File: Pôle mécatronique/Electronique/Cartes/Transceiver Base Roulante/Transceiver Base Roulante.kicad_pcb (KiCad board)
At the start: 2 copper layers, 18.8 x 30.7 mm, 6 parts, among them J1 Conn_01x02, J3 Conn_01x01, J4 Conn_01x01, J6 Conn_01x02, U1 TCAN332

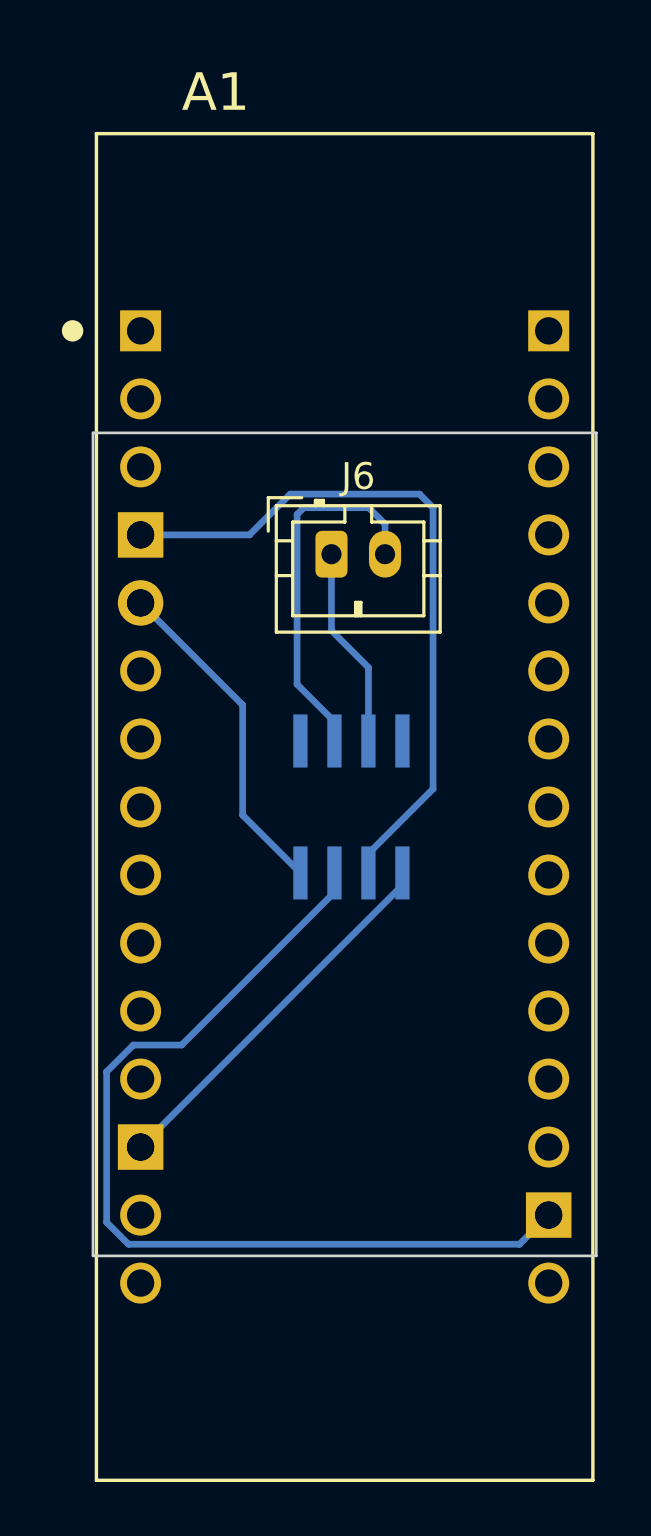
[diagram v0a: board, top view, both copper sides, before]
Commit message: Carte transceiver base roulante update
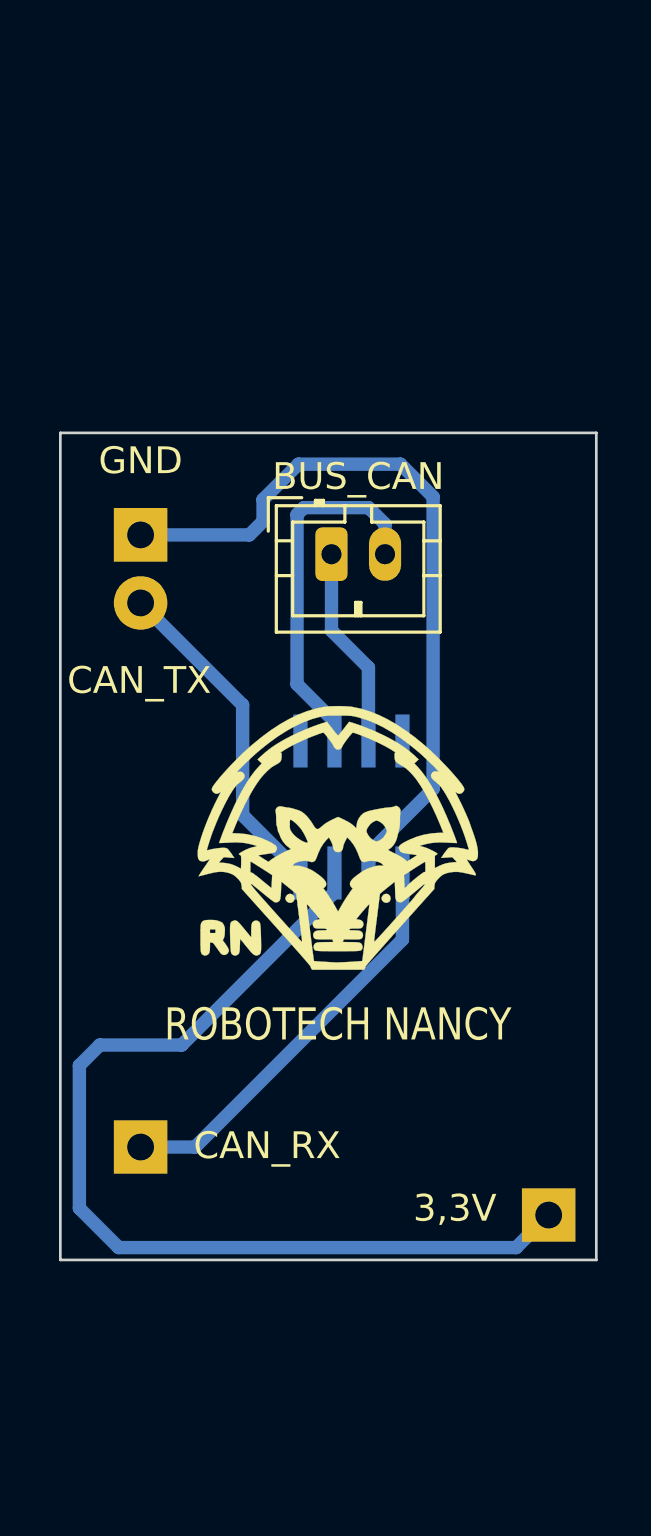
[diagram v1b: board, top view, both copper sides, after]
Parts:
- removed A1: NUCLEO-F303K8, empreinte:MODULE_NUCLEO-F303K8
- added G***: LOGO, Logos:logoRobotechNancy10x10, F.Cu at (154.4, 74.9)
- renumbered J3 to 3,3V, J6 to BUS_CAN, J4 to CAN_RX, J1 to GND
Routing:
- net +3V3: track 34.9 -> 36.9 mm
- net GND: track 26.4 -> 28.0 mm
- net CAN_RX: track 14.3 -> 15.5 mm
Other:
- board size 18.8 x 30.7 mm -> 20 x 30.9 mm
- board text added: "CAN_TX"
- board text added: "ROBOTECH NANCY"

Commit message: TCAN base roulante update
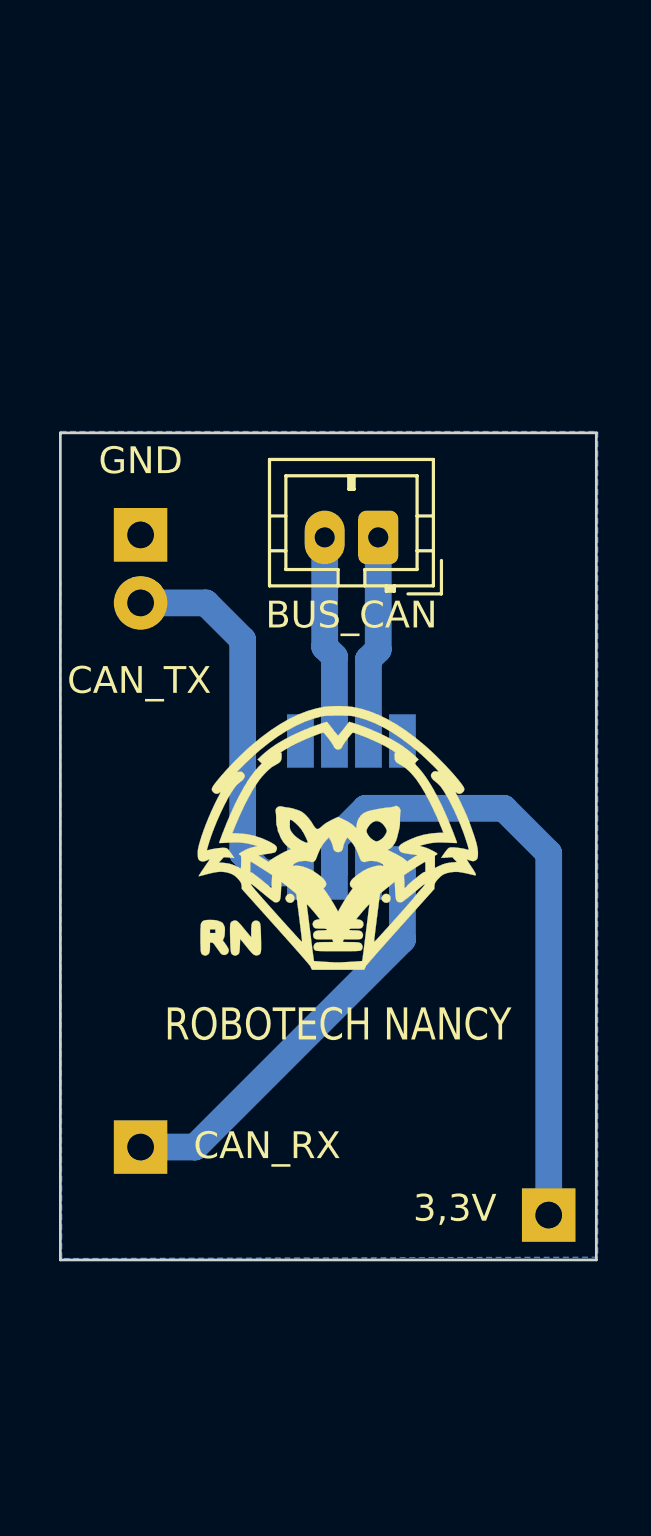
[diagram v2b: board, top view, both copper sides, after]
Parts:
- moved BUS_CAN 1.86 mm to (155.9, 63.8), turned to 180 degrees
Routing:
- net GND: track 28.0 -> 0.00 mm
- net +3V3: track 36.9 -> 23.9 mm
- net CAN_L: track 13.8 -> 7.75 mm
- net CAN_TX: track 12.6 -> 14.8 mm
- added copper zone on B.Cu, net GND
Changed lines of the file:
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@@
   )
   (setup
+    (stackup
+      (layer "F.SilkS" (type "Top Silk Screen"))
+      (layer "F.Paste" (type "Top Solder Paste"))
+      (layer "F.Mask" (type "Top Solder Mask") (thickness 0.01))
+      (layer "F.Cu" (type "copper") (thickness 0.035))
+      (layer "dielectric 1" (type "core") (thickness 1.51) (material "FR4") (epsilon_r 4.5) (loss_tangent 0.02))
+      (layer "B.Cu" (type "copper") (thickness 0.035))
+      (layer "B.Mask" (type "Bottom Solder Mask") (thickness 0.01))
+      (layer "B.Paste" (type "Bottom Solder Paste"))
+      (layer "B.SilkS" (type "Bottom Silk Screen"))
+      (copper_finish "None")
+      (dielectric_constraints no)
+    )
     (pad_to_mask_clearance 0)
     (pcbplotparams
@@
   (net 8 "unconnected-(U1-Pad8)")
   (footprint "Connector_JST:JST_PH_B2B-PH-K_1x02_P2.00mm_Vertical" (layer "F.Cu")
-    (at 154.194 64.474)
+    (at 155.94 63.8468 180)
     (descr "JST PH series connector, B2B-PH-K (http://www.jst-mfg.com/product/pdf/eng/ePH.pdf), generated with kicad-footprint-generator")
     (tags "connector JST PH side entry")
@@
     (fp_line (start -1.95 -1.7) (end -1.95 2.8) (layer "F.Fab") (width 0.1))
     (fp_line (start -1.11 -2.11) (end -2.36 -2.11) (layer "F.Fab") (width 0.1))
-    (pad "1" thru_hole roundrect locked (at 0 0) (size 1.2 2) (drill 0.75) (layers *.Cu *.Mask) (roundrect_rratio 0.208333)
+    (pad "1" thru_hole roundrect locked (at 0 0 180) (size 1.5 2) (drill 0.75) (layers *.Cu *.Mask) (roundrect_rratio 0.208333)
       (net 7 "CAN_H") (pinfunction "Pin_1") (pintype "passive"))
-    (pad "2" thru_hole oval locked (at 2 0) (size 1.2 2) (drill 0.75) (layers *.Cu *.Mask)
+    (pad "2" thru_hole oval locked (at 2 0 180) (size 1.5 2) (drill 0.75) (layers *.Cu *.Mask)
       (net 6 "CAN_L") (pinfunction "Pin_2") (pintype "passive"))
     (model "${KICAD6_3DMODEL_DIR}/Connector_JST.3dshapes/JST_PH_B2B-PH-K_1x02_P2.00mm_Vertical.wrl"
@@
     (fp_line (start 3.0988 0.4064) (end 3.0988 0.889) (layer "B.Fab") (width 0.1524))
     (fp_arc (start -0.3048 2.4892) (mid 0.0127 2.1971) (end 0.3048 2.5146) (layer "B.Fab") (width 0.1524))
-    (pad "1" smd rect locked (at -2.4638 1.905 90) (size 1.9812 0.5334) (layers "B.Cu" "B.Paste" "B.Mask")
+    (pad "1" smd rect locked (at -2.4638 1.905 90) (size 2 1) (layers "B.Cu" "B.Paste" "B.Mask")
       (net 2 "CAN_RX") (pinfunction "TXD") (pintype "input"))
-    (pad "2" smd rect locked (at -2.4638 0.635 90) (size 1.9812 0.5334) (layers "B.Cu" "B.Paste" "B.Mask")
+    (pad "2" smd rect locked (at -2.4638 0.635 90) (size 2 1) (layers "B.Cu" "B.Paste" "B.Mask")
       (net 1 "GND") (pinfunction "GND") (pintype "power_in"))
-    (pad "3" smd rect locked (at -2.4638 -0.635 90) (size 1.9812 0.5334) (layers "B.Cu" "B.Paste" "B.Mask")
+    (pad "3" smd rect locked (at -2.4638 -0.635 90) (size 2 1) (layers "B.Cu" "B.Paste" "B.Mask")
       (net 4 "+3V3") (pinfunction "VCC") (pintype "power_in"))
-    (pad "4" smd rect locked (at -2.4638 -1.905 90) (size 1.9812 0.5334) (layers "B.Cu" "B.Paste" "B.Mask")
+    (pad "4" smd rect locked (at -2.4638 -1.905 90) (size 2 1) (layers "B.Cu" "B.Paste" "B.Mask")
       (net 3 "CAN_TX") (pinfunction "RXD") (pintype "tri_state"))
-    (pad "5" smd rect locked (at 2.4638 -1.905 90) (size 1.9812 0.5334) (layers "B.Cu" "B.Paste" "B.Mask")
+    (pad "5" smd rect locked (at 2.4638 -1.905 90) (size 2 1) (layers "B.Cu" "B.Paste" "B.Mask")
       (net 5 "unconnected-(U1-Pad5)") (pinfunction "NC") (pintype "no_connect"))
-    (pad "6" smd rect locked (at 2.4638 -0.635 90) (size 1.9812 0.5334) (layers "B.Cu" "B.Paste" "B.Mask")
+    (pad "6" smd rect locked (at 2.4638 -0.635 90) (size 2 1) (layers "B.Cu" "B.Paste" "B.Mask")
       (net 6 "CAN_L") (pinfunction "CANL") (pintype "bidirectional"))
-    (pad "7" smd rect locked (at 2.4638 0.635 90) (size 1.9812 0.5334) (layers "B.Cu" "B.Paste" "B.Mask")
+    (pad "7" smd rect locked (at 2.4638 0.635 90) (size 2 1) (layers "B.Cu" "B.Paste" "B.Mask")
       (net 7 "CAN_H") (pinfunction "CANH") (pintype "bidirectional"))
-    (pad "8" smd rect locked (at 2.4638 1.905 90) (size 1.9812 0.5334) (layers "B.Cu" "B.Paste" "B.Mask")
+    (pad "8" smd rect locked (at 2.4638 1.905 90) (size 2 1) (layers "B.Cu" "B.Paste" "B.Mask")
       (net 8 "unconnected-(U1-Pad8)") (pinfunction "NC") (pintype "no_connect"))
     (model "C:/Users/tomro/OneDrive/Documents/Kicad/3D/LTC1329CS8-50#PBF.STEP"
@@
     (effects (font (size 1.2 1) (thickness 0.25)))
   )
-  (segment (start 152.9588 61.1124) (end 151.638 62.4332) (width 0.5) (layer "B.Cu") (net 1))
-  (segment (start 151.638 62.4332) (end 151.638 63.246) (width 0.5) (layer "B.Cu") (net 1))
-  (segment (start 155.575 75.6539) (end 157.988 73.2409) (width 0.5) (layer "B.Cu") (net 1))
-  (segment (start 156.7688 61.1124) (end 152.9588 61.1124) (width 0.5) (layer "B.Cu") (net 1))
-  (segment (start 151.638 63.246) (end 151.13 63.754) (width 0.5) (layer "B.Cu") (net 1))
-  (segment (start 157.988 73.2409) (end 157.988 62.3316) (width 0.5) (layer "B.Cu") (net 1))
-  (segment (start 157.988 62.3316) (end 156.7688 61.1124) (width 0.5) (layer "B.Cu") (net 1))
-  (segment (start 151.13 63.754) (end 147.066 63.754) (width 0.5) (layer "B.Cu") (net 1))
-  (segment (start 155.575 76.3778) (end 155.575 75.6539) (width 0.5) (layer "B.Cu") (net 1))
-  (segment (start 147.066 86.614) (end 149.098 86.614) (width 0.5) (layer "B.Cu") (net 2))
-  (segment (start 149.098 86.614) (end 156.845 78.867) (width 0.5) (layer "B.Cu") (net 2))
-  (segment (start 156.845 78.867) (end 156.845 76.3778) (width 0.5) (layer "B.Cu") (net 2))
-  (segment (start 150.876 70.104) (end 150.876 74.2188) (width 0.5) (layer "B.Cu") (net 3))
-  (segment (start 147.066 66.294) (end 150.876 70.104) (width 0.5) (layer "B.Cu") (net 3))
-  (segment (start 150.876 74.2188) (end 153.035 76.3778) (width 0.5) (layer "B.Cu") (net 3))
-  (segment (start 148.6027 82.804) (end 154.305 77.1017) (width 0.5) (layer "B.Cu") (net 4))
-  (segment (start 144.78 83.566) (end 145.542 82.804) (width 0.5) (layer "B.Cu") (net 4))
-  (segment (start 144.78 88.9) (end 144.78 83.566) (width 0.5) (layer "B.Cu") (net 4))
-  (segment (start 154.305 77.1017) (end 154.305 76.3778) (width 0.5) (layer "B.Cu") (net 4))
-  (segment (start 162.306 89.154) (end 161.091489 90.368511) (width 0.5) (layer "B.Cu") (net 4))
-  (segment (start 161.091489 90.368511) (end 146.248511 90.368511) (width 0.5) (layer "B.Cu") (net 4))
-  (segment (start 146.248511 90.368511) (end 144.78 88.9) (width 0.5) (layer "B.Cu") (net 4))
-  (segment (start 145.542 82.804) (end 148.6027 82.804) (width 0.5) (layer "B.Cu") (net 4))
-  (segment (start 155.583 62.738) (end 153.162 62.738) (width 0.5) (layer "B.Cu") (net 6))
-  (segment (start 156.194 64.474) (end 156.194 63.349) (width 0.5) (layer "B.Cu") (net 6))
-  (segment (start 152.908 69.3293) (end 154.305 70.7263) (width 0.5) (layer "B.Cu") (net 6))
-  (segment (start 154.305 70.7263) (end 154.305 71.4502) (width 0.5) (layer "B.Cu") (net 6))
-  (segment (start 156.194 63.349) (end 155.583 62.738) (width 0.5) (layer "B.Cu") (net 6))
-  (segment (start 153.162 62.738) (end 152.908 62.992) (width 0.5) (layer "B.Cu") (net 6))
-  (segment (start 152.908 62.992) (end 152.908 69.3293) (width 0.5) (layer "B.Cu") (net 6))
-  (segment (start 154.194 67.326) (end 155.575 68.707) (width 0.5) (layer "B.Cu") (net 7))
-  (segment (start 155.575 68.707) (end 155.575 71.4502) (width 0.5) (layer "B.Cu") (net 7))
-  (segment (start 154.194 64.474) (end 154.194 67.326) (width 0.5) (layer "B.Cu") (net 7))
+  (segment (start 147.066 86.614) (end 149.098 86.614) (width 1) (layer "B.Cu") (net 2))
+  (segment (start 149.098 86.614) (end 156.845 78.867) (width 1) (layer "B.Cu") (net 2))
+  (segment (start 156.845 78.867) (end 156.845 76.3778) (width 1) (layer "B.Cu") (net 2))
+  (segment (start 150.876 67.6656) (end 150.876 75.6412) (width 1) (layer "B.Cu") (net 3))
+  (segment (start 149.5044 66.294) (end 150.876 67.6656) (width 1) (layer "B.Cu") (net 3))
+  (segment (start 147.066 66.294) (end 149.5044 66.294) (width 1) (layer "B.Cu") (net 3))
+  (segment (start 151.6126 76.3778) (end 153.035 76.3778) (width 1) (layer "B.Cu") (net 3))
+  (segment (start 150.876 75.6412) (end 151.6126 76.3778) (width 1) (layer "B.Cu") (net 3))
+  (segment (start 162.306 75.6412) (end 160.6296 73.9648) (width 1) (layer "B.Cu") (net 4))
+  (segment (start 155.468 73.9648) (end 154.305 75.1278) (width 1) (layer "B.Cu") (net 4))
+  (segment (start 160.6296 73.9648) (end 155.468 73.9648) (width 1) (layer "B.Cu") (net 4))
+  (segment (start 162.306 89.154) (end 162.306 75.6412) (width 1) (layer "B.Cu") (net 4))
+  (segment (start 154.305 75.1278) (end 154.305 76.3778) (width 1) (layer "B.Cu") (net 4))
+  (segment (start 154.305 71.4502) (end 154.305 68.3006) (width 1) (layer "B.Cu") (net 6))
+  (segment (start 153.94 67.9356) (end 153.94 63.8468) (width 1) (layer "B.Cu") (net 6))
+  (segment (start 154.305 68.3006) (end 153.94 67.9356) (width 1) (layer "B.Cu") (net 6))
+  (segment (start 155.94 68.0372) (end 155.575 68.4022) (width 1) (layer "B.Cu") (net 7))
+  (segment (start 155.94 63.8468) (end 155.94 68.0372) (width 1) (layer "B.Cu") (net 7))
+  (segment (start 155.575 68.4022) (end 155.575 71.4502) (width 1) (layer "B.Cu") (net 7))
+  (zone (net 1) (net_name "GND") (layer "B.Cu") (hatch none 0.508)
+    (connect_pads (clearance 0.508))
+    (min_thickness 0.254) (filled_areas_thickness no)
+    (fill yes (thermal_gap 0.508) (thermal_bridge_width 0.508))
+    (polygon
+      (pts
+        (xy 164.1348 90.7288)
+        (xy 144.1196 90.7796)
+        (xy 144.0688 59.8932)
+        (xy 164.1348 59.8932)
+      )
+    )
+  )
 )
